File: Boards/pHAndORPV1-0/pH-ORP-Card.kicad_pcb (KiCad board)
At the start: 4 copper layers, 80 x 72 mm, 110 parts, among them IC1 PIC32MM0064GPM028, P1 ICSP, P2 AquaPicBus, P3 2x1 2.54, P4 pH, P5 pH/ORP, Q1 NX7002AK, Q2 NX7002AK, Q3 NX7002AK, Q4 AO3407A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

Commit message: worked on pH ORP board layout
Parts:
- moved U1 125.3 mm to (6.99, -48.3)
- moved Q1 112.8 mm to (116.8, -40.6)
- moved R35 86.4 mm to (67.3, -36.2)
- moved R37 78.0 mm to (75.6, -16.5)
- moved U12 64.3 mm to (71.8, -9.14), turned to 90 degrees
- moved C26 50.3 mm to (68.6, -27.3)
- moved R31 42.2 mm to (62.2, -31.1), turned to 270 degrees
- moved C22 41.3 mm to (52.7, -30.5)
- moved C23 38.8 mm to (61.6, -26.7)
- moved R38 38.0 mm to (71.8, -16.5), turned to 180 degrees
- moved C34 37.5 mm to (76.2, -10.8), turned to 90 degrees
- moved C30 35.1 mm to (102.9, -19.7)
- moved R34 34.7 mm to (76.2, -33.0)
- moved R33 34.3 mm to (64.8, -31.1)
- moved R29 23.7 mm to (54.0, -24.8), turned to 180 degrees
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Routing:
- net GNDA: track 66.5 -> 30.0 mm, vias 11 -> 20
- net (no net): track 20.5 -> 0.00 mm, vias 7 -> 0
- net Net-(C22-Pad2): track 3.96 -> 20.5 mm, vias 2 -> 0
- net Net-(R34-Pad1): track 0.00 -> 14.4 mm
- net Net-(D4-Pad1): track 0.85 -> 13.4 mm, vias 1 -> 0
- net Net-(R39-Pad2): track 0.75 -> 13.0 mm
- net Net-(C22-Pad1): track 8.07 -> 19.3 mm, vias 0 -> 2
- net -5VA: track 6.71 -> 17.7 mm, vias 2 -> 5
- net /A_pH/ORP: track 6.61 -> 17.4 mm
- net Net-(R29-Pad1): track 14.4 -> 3.67 mm
- net Net-(R40-Pad2): track 0.00 -> 9.75 mm
- net Net-(C25-Pad1): track 1.36 -> 9.33 mm, vias 1 -> 0
- net Net-(C27-Pad2): track 1.58 -> 8.86 mm, vias 1 -> 0
- net Net-(U8-Pad5): track 6.91 -> 0.00 mm
- net +5VA: track 47.6 -> 43.2 mm, vias 8 -> 12
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
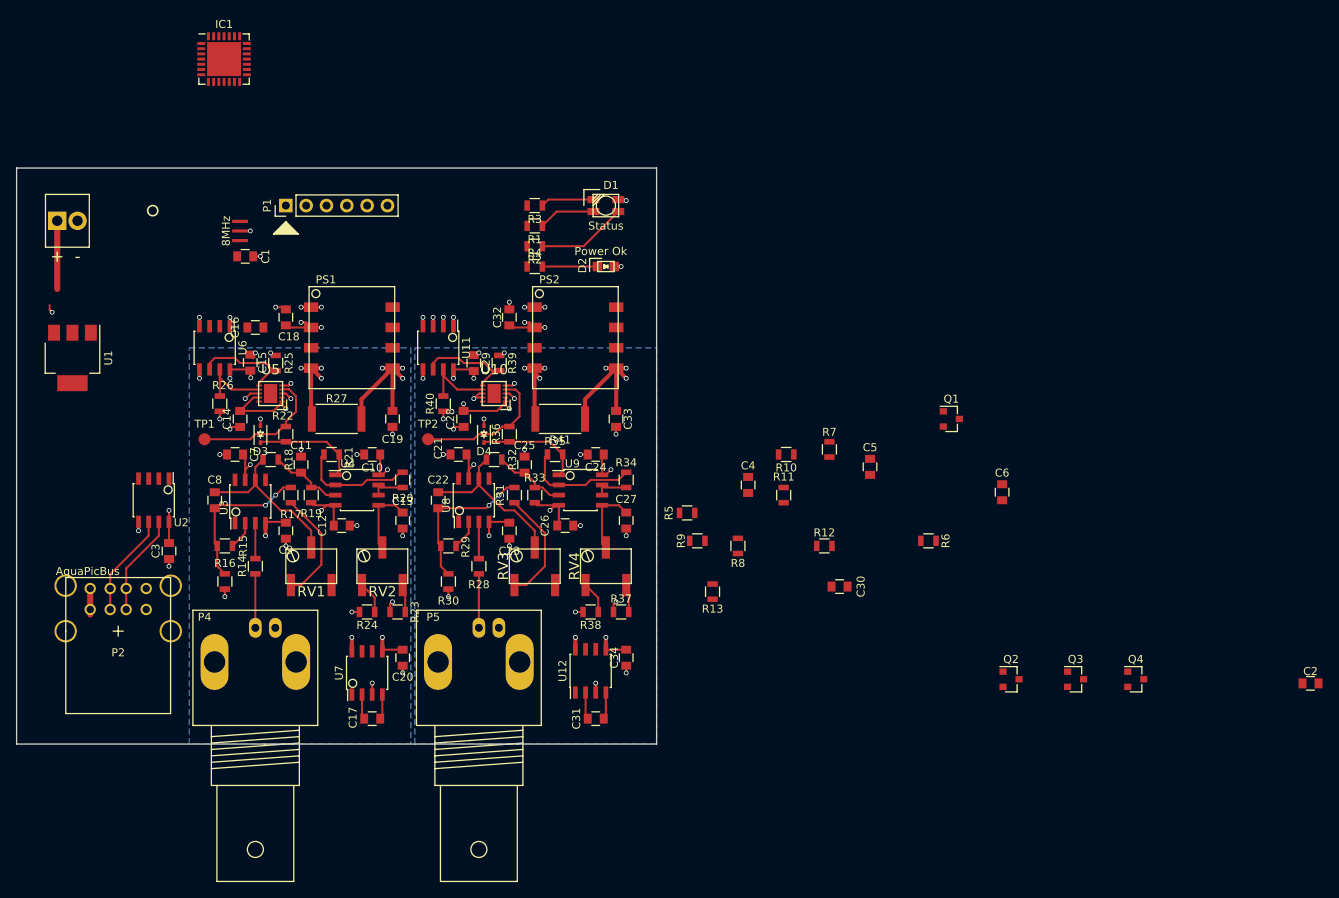
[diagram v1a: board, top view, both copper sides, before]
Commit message: added firmware for the pH ORP Card
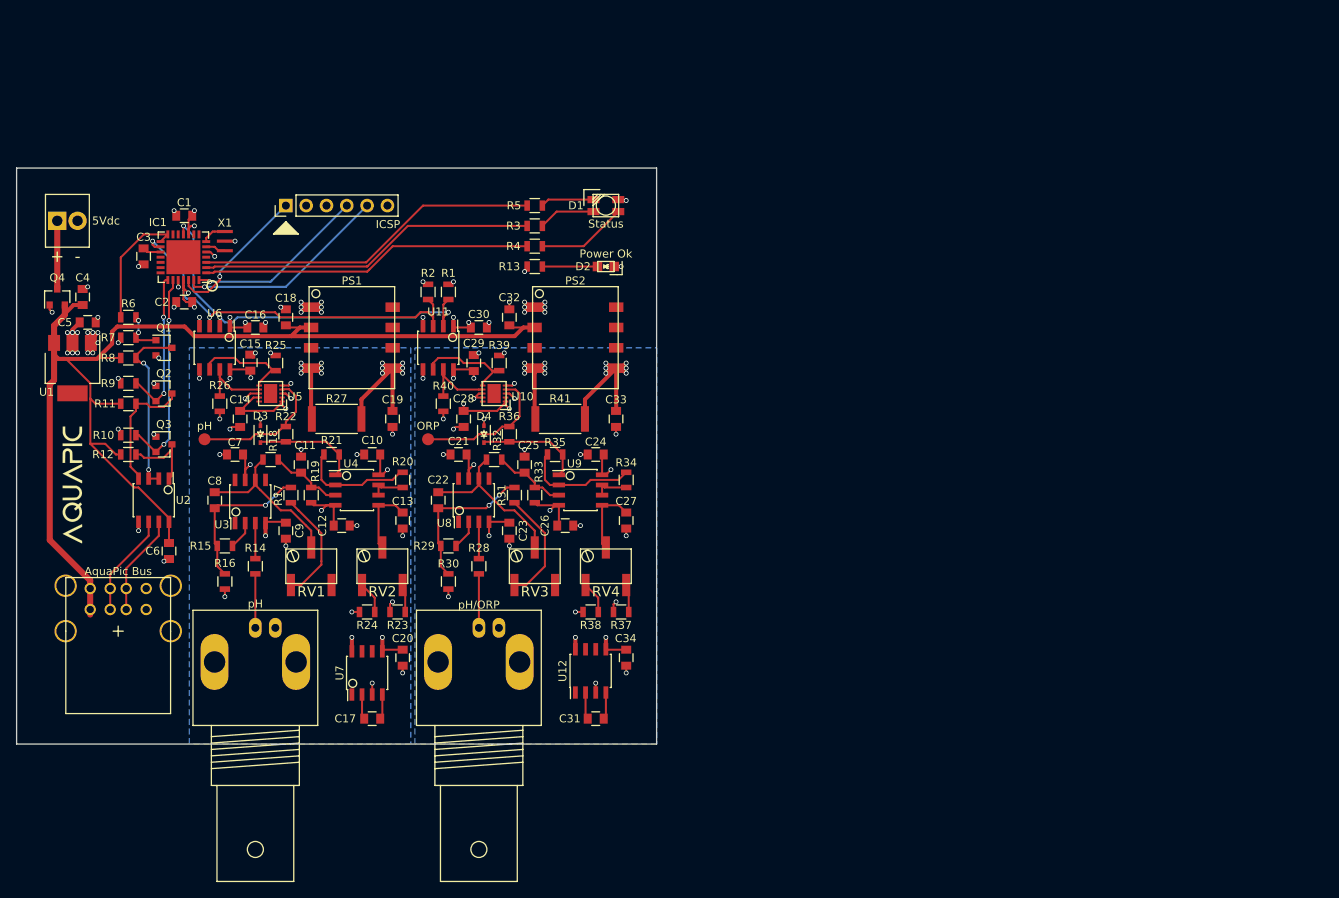
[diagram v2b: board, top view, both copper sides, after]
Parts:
- added G***: LOGO, MyFootPrints:AquaPic_Logo_Small, F.Cu at (6.99, -32.4)
- added REF***: OSHW-Logo2_14.6x12mm_SilkScreen, Symbols:OSHW-Logo2_14.6x12mm_SilkScreen, B.Cu at (54.0, -25.4)
- AquaPic Bus: renamed from P2; value AquaPicBus -> usb1.1
- ICSP: renamed from P1; value ICSP -> 5x1 2.54
- pH: renamed from P4; value pH -> BNC
- pH/ORP: renamed from P5; value pH/ORP -> BNC
- moved C2 148.6 mm to (21.0, -55.2), turned to 180 degrees
- moved Q4 143.0 mm to (5.08, -55.9), turned to 90 degrees
- moved Q3 117.7 mm to (18.4, -37.5)
- moved Q2 111.8 mm to (18.4, -43.8)
- moved C6 104.4 mm to (19.1, -24.1)
- moved R6 103.8 mm to (14.0, -53.3), turned to 180 degrees
- moved C5 99.4 mm to (8.89, -52.7), turned to 0 degrees
- moved Q1 98.8 mm to (18.4, -49.5)
- moved R7 88.7 mm to (14.0, -50.8), turned to 180 degrees
- moved R12 87.7 mm to (14.0, -36.2)
- moved C4 86.4 mm to (8.26, -55.9)
- moved R11 82.7 mm to (14.0, -42.5), turned to 0 degrees
- moved R10 82.3 mm to (14.0, -38.6), turned to 0 degrees
- moved R8 79.7 mm to (14.0, -48.3), turned to 0 degrees
- moved R9 73.8 mm to (14.0, -45.1), turned to 0 degrees
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- renumbered P3 to 5Vdc, TP2 to ORP, TP1 to pH
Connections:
- IC1 pad 1: /LED_R -> /LED_Y
- IC1 pad 3: /LED_Y -> /LED_R
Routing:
- net +5V: track 18.8 -> 171.3 mm, vias 5 -> 0
- net /SDA: track 1.11 -> 50.5 mm, vias 1 -> 3
- net /SCL: track 1.11 -> 48.3 mm, vias 1 -> 2
- net /LED_R: track 0.00 -> 43.1 mm
- net /LED_G: track 0.00 -> 42.3 mm
- net /LED_Y: track 6.89 -> 41.5 mm
- net /PGC: track 0.00 -> 26.7 mm, vias 0 -> 1
- net GND: track 14.7 -> 40.7 mm, vias 13 -> 38
- net /RX_LV: track 0.00 -> 25.8 mm, vias 0 -> 2
- net +3V3: track 10.9 -> 35.6 mm, vias 3 -> 22
- net /PGD: track 0.00 -> 22.5 mm, vias 0 -> 1
- net /RTS: track 0.00 -> 22.4 mm, vias 0 -> 2
- net /TX_LV: track 0.00 -> 19.4 mm, vias 0 -> 2
- net //MCLR: track 0.00 -> 18.5 mm, vias 0 -> 1
- net //RTS: track 0.00 -> 15.8 mm
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- added copper zone on In2.Cu, net +3V3
- removed copper zone on In2.Cu, net +5V
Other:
- net class Default: clearance 0.2032 -> 0.1524
- rule trace_clearance: 0.2032 -> 0.1524
- board text added: "AquaPic pH and ORP Rev 1 Goodtime Development Skyler Brandt"
- board text removed: "AquaPic pH and ORP Rev 0 Skyler"

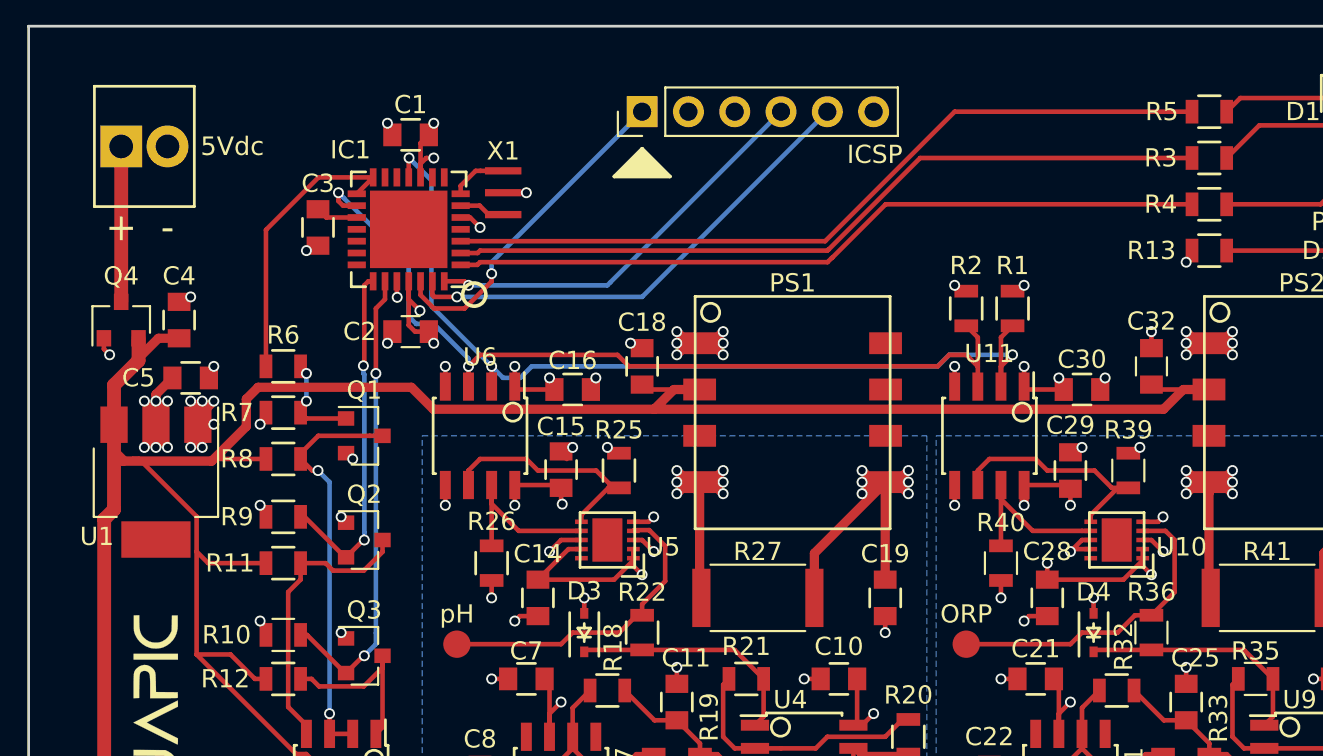
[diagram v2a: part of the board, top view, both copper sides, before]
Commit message: added enable disable for ph isolation
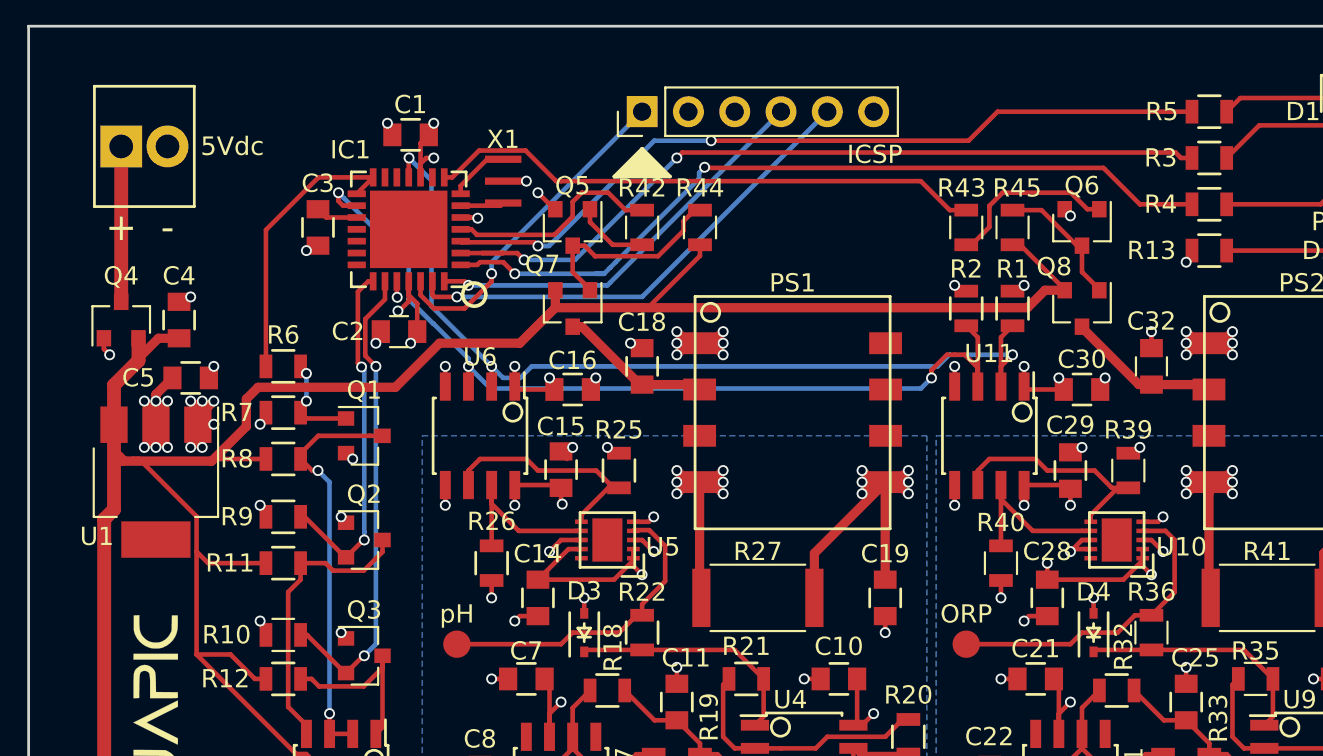
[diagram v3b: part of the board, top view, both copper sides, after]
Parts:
- added Q5: MMBT3904, TO_SOT_Packages_SMD:SOT-23, F.Cu at (29.8, -61.0)
- added Q6: MMBT3904, TO_SOT_Packages_SMD:SOT-23, F.Cu at (57.8, -61.0)
- added Q7: AO3407A, TO_SOT_Packages_SMD:SOT-23, F.Cu at (29.8, -56.5)
- added Q8: AO3407A, TO_SOT_Packages_SMD:SOT-23, F.Cu at (57.8, -56.5)
- added R42: 1K, Resistors_SMD:R_0805, F.Cu at (33.7, -61.0)
- added R43: 1K, Resistors_SMD:R_0805, F.Cu at (51.4, -61.0)
- added R44: 10K, Resistors_SMD:R_0805, F.Cu at (36.8, -61.0)
- added R45: 10K, Resistors_SMD:R_0805, F.Cu at (54.0, -61.0)
- D1: value SMP4-RGY -> SMTL4-RGY
- moved C2 0.63 mm to (20.3, -55.2)
- moved X1 0.63 mm to (26.0, -63.5)
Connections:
- C18 pad 1: +5V -> Net-(C18-Pad1)
- C32 pad 1: +5V -> Net-(C32-Pad1)
- IC1 pad 4: Net-(IC1-Pad4) -> /En_pH
- IC1 pad 8: Net-(IC1-Pad8) -> /En_pH/ORP
- PS1 pad 2: +5V -> Net-(C18-Pad1)
- PS2 pad 2: +5V -> Net-(C32-Pad1)
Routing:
- net /En_pH/ORP: track 0.00 -> 30.6 mm
- net /En_pH: track 0.00 -> 11.9 mm
- net Net-(Q5-Pad3): track 0.00 -> 11.4 mm
- net Net-(Q6-Pad1): track 0.00 -> 9.54 mm
- net Net-(C32-Pad1): track 0.00 -> 8.80 mm
- net Net-(C18-Pad1): track 0.00 -> 8.65 mm
- net Net-(Q6-Pad3): track 0.00 -> 7.46 mm
- net +5V: track 171.3 -> 164.7 mm
- net Net-(Q5-Pad1): track 0.00 -> 4.08 mm
- net /LED_Y: track 41.5 -> 44.3 mm, vias 0 -> 2
- net GND: track 40.7 -> 42.7 mm, vias 38 -> 40
- net /LED_G: track 42.3 -> 44.3 mm, vias 0 -> 2
- net /SCL: track 48.3 -> 49.5 mm, vias 2 -> 3
- net +3V3: track 35.6 -> 34.9 mm
- net /LED_R: track 43.1 -> 43.3 mm, vias 0 -> 2

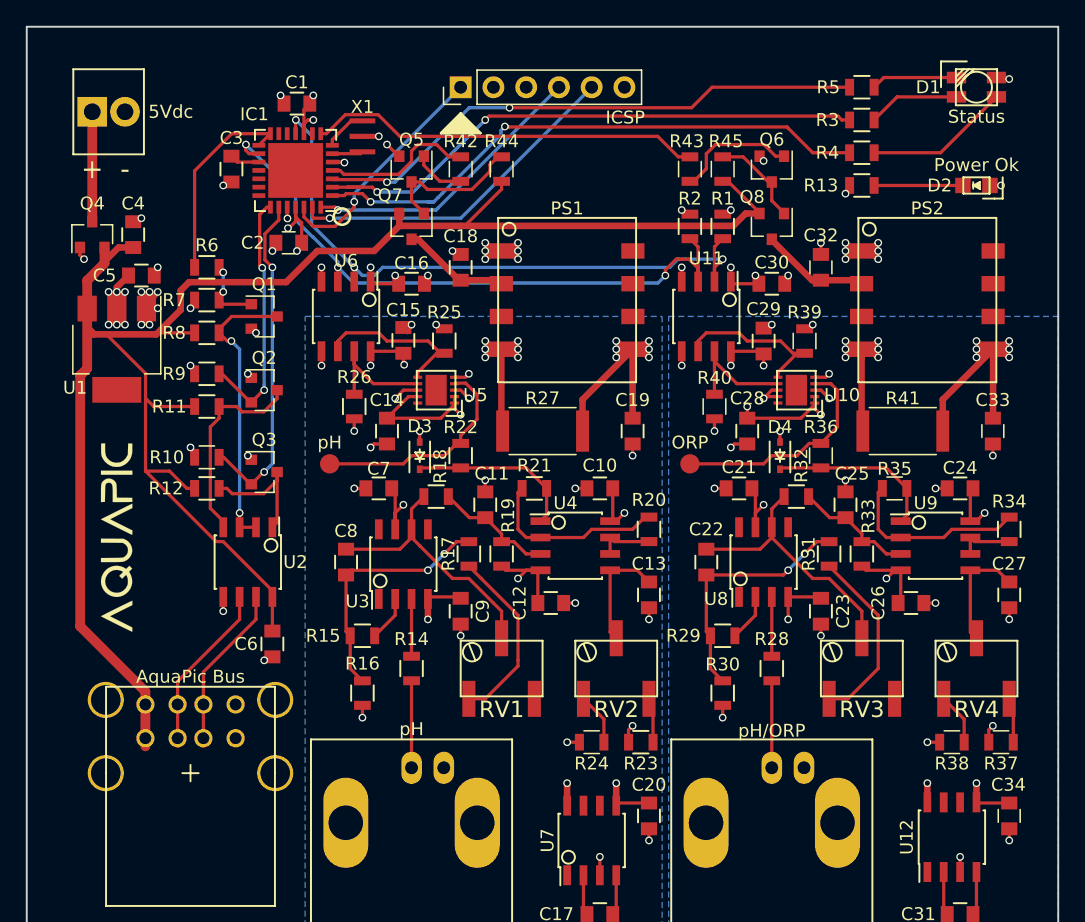
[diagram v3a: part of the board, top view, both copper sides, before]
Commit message: fixed placement on boards so everything is mostly in the same spot
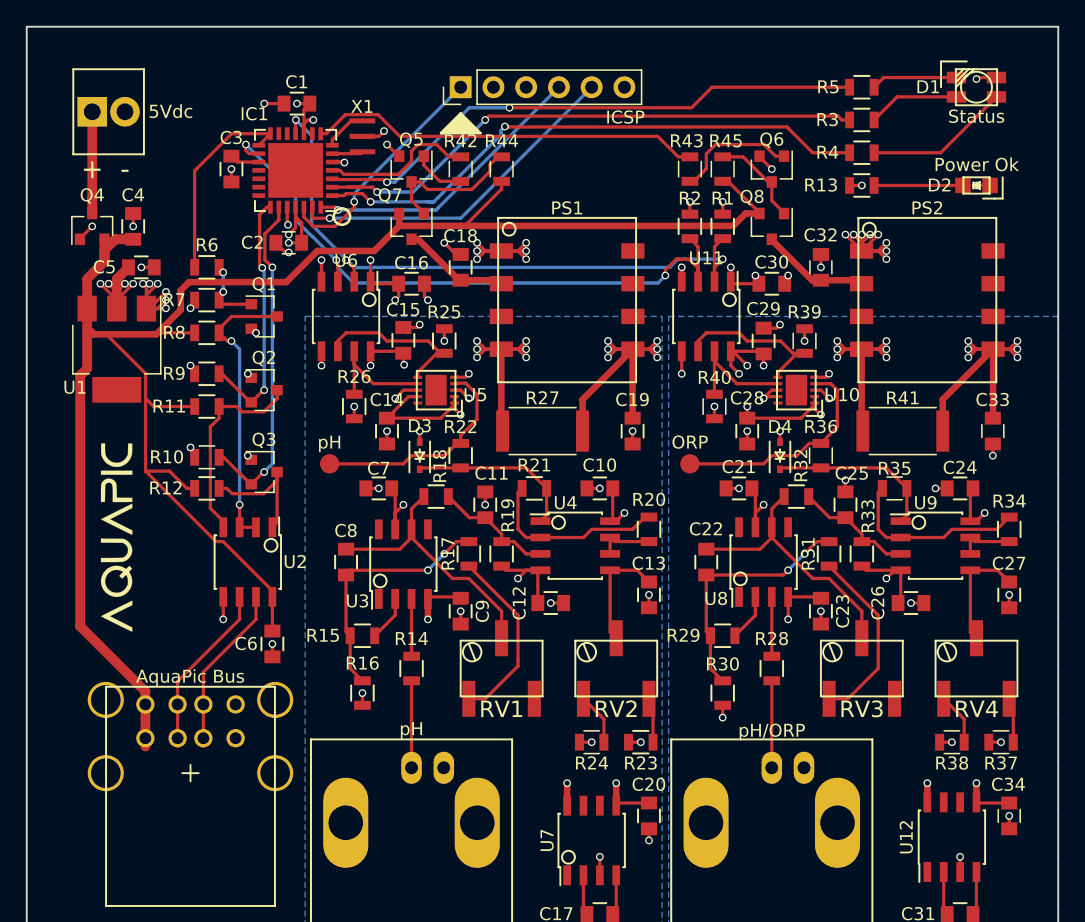
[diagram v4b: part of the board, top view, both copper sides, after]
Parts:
- moved C5 0.64 mm to (8.89, -53.3)
- moved C4 0.63 mm to (8.26, -56.5)
- moved Q4 0.63 mm to (5.08, -56.5)
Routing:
- net GND: track 42.7 -> 67.3 mm, vias 40 -> 42
- net +5VA: track 46.3 -> 52.6 mm, vias 15 -> 16
- net +3V3: track 34.9 -> 41.1 mm, vias 22 -> 20
- net GNDA: track 34.0 -> 39.1 mm
- net GNDD: track 33.1 -> 37.7 mm
- net +5VD: track 50.7 -> 55.0 mm
- net /SCL: track 49.5 -> 50.3 mm
- net Net-(P3-Pad1): track 8.52 -> 7.89 mm
- net +5V: track 164.7 -> 164.1 mm
